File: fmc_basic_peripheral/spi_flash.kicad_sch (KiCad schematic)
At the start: 4 parts, among them J2 ACA-SPI-004-K02, U12 TPD4E02B04DQA

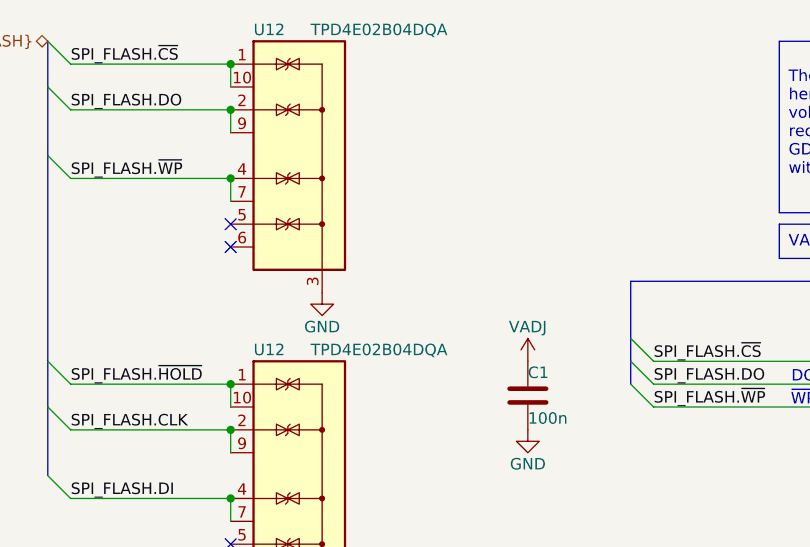
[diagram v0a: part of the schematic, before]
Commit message: fmc_basic_peripheral: Migrate to kicad8
- Migrate schematics to kicad8
- Migrate PCB to kicad8
- Clean ERC
- Clean LVS and DRC

Signed-off-by: Huang Rui <vowstar@gmail.com>
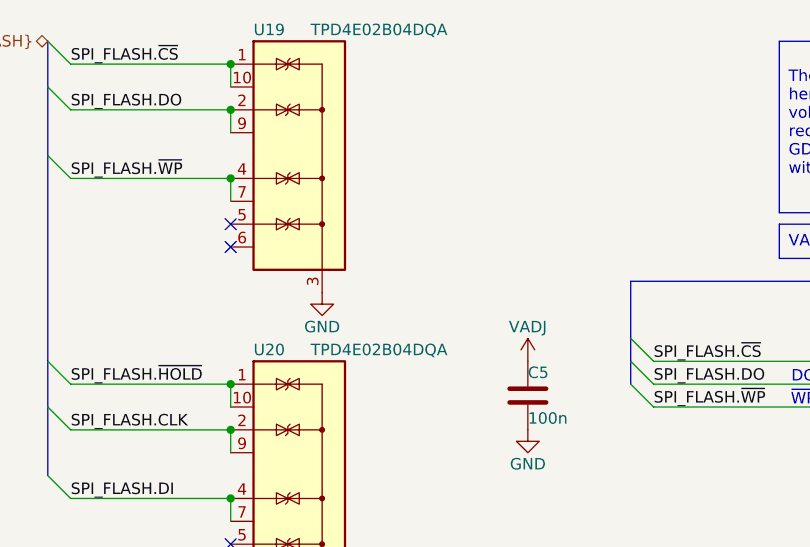
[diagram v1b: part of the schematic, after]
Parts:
- renumbered C1 to C5, U12 to U19, U12 to U20
